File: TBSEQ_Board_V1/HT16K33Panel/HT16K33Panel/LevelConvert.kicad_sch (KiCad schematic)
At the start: 4 parts, among them J14 Conn_01x04_Pin, J3 Conn_01x04_Pin, U4 AE-LCNV4-MOSFET, U5 74HC126

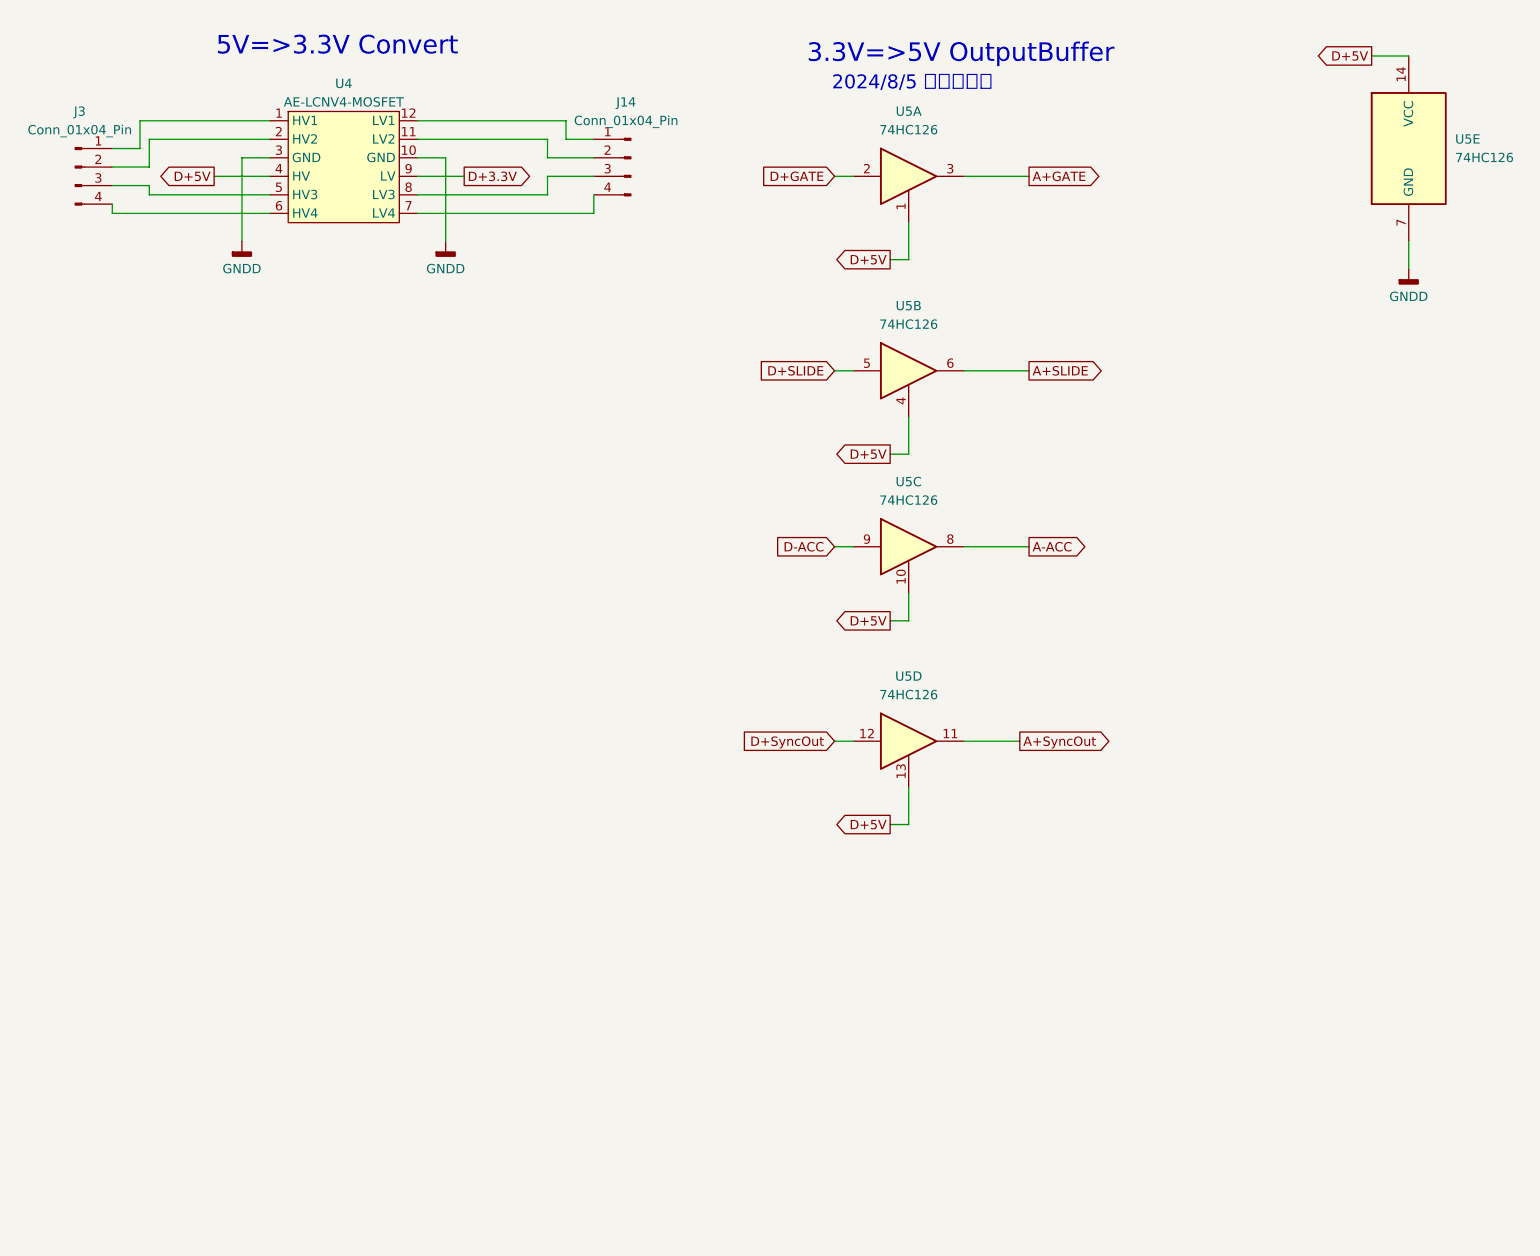
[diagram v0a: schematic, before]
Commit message: HT16K33Panel LevelConvert
HD74LVC541A で5V->3.3Vへ変換をブレッドボードで確認済
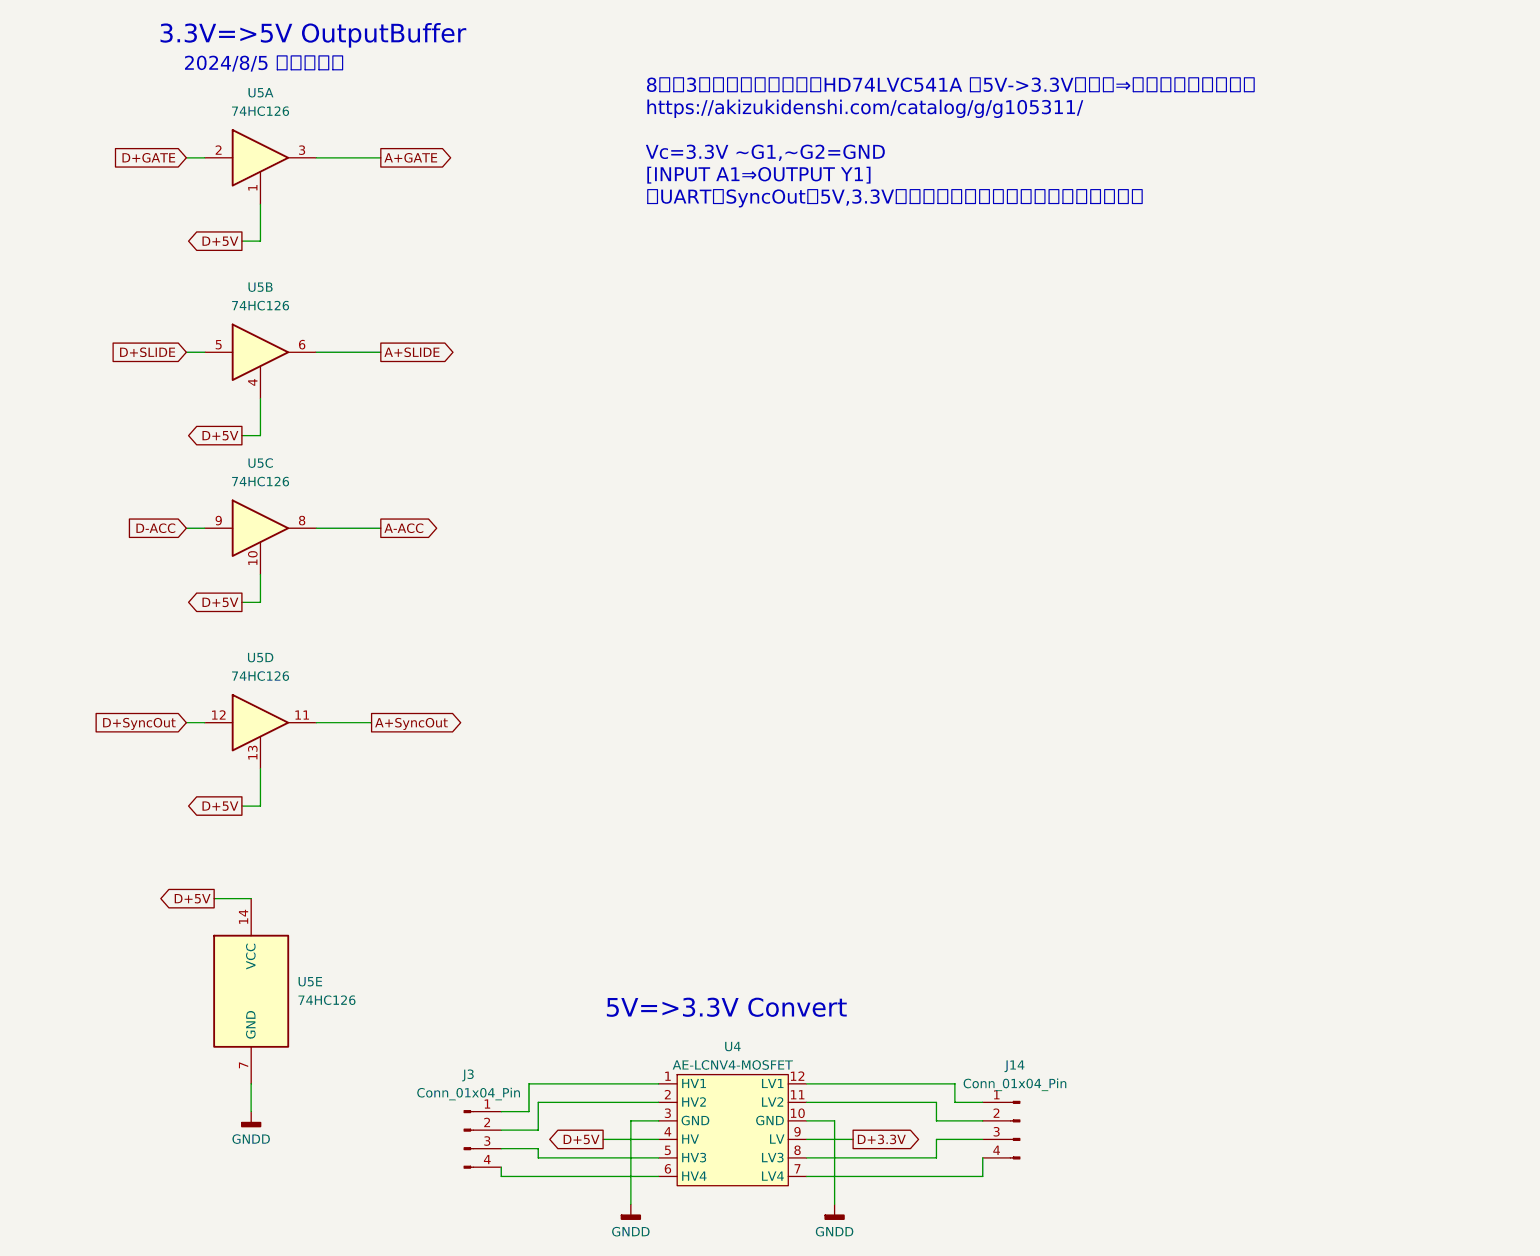
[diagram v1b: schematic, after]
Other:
- note added: "8回路3ステートバッファーHD74LVC541A で5V->3.3Vへ変換⇒こっちに置き換える https://akizukidenshi.com/catalog/g/g105311/ Vc=3.3V ~G1,~G2=GND [INPUT A1⇒OUTPUT Y1] ・UARTとSyncOutで5V,3.3Vともに同じ波形が出力される事を確認済"
- moved on the sheet: J14, J3, U4, U5A, U5B, U5C, U5D, U5E
